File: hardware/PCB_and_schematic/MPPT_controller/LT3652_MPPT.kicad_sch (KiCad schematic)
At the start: 36 parts, among them J10 RS485, J8 ICP, J9 Conn_01x03, Q17 BC817, Q18 BC817, Q19 BC817, Q20 BC817, U1 LT3652EMSE, U5 TL431LP, U6 ST485

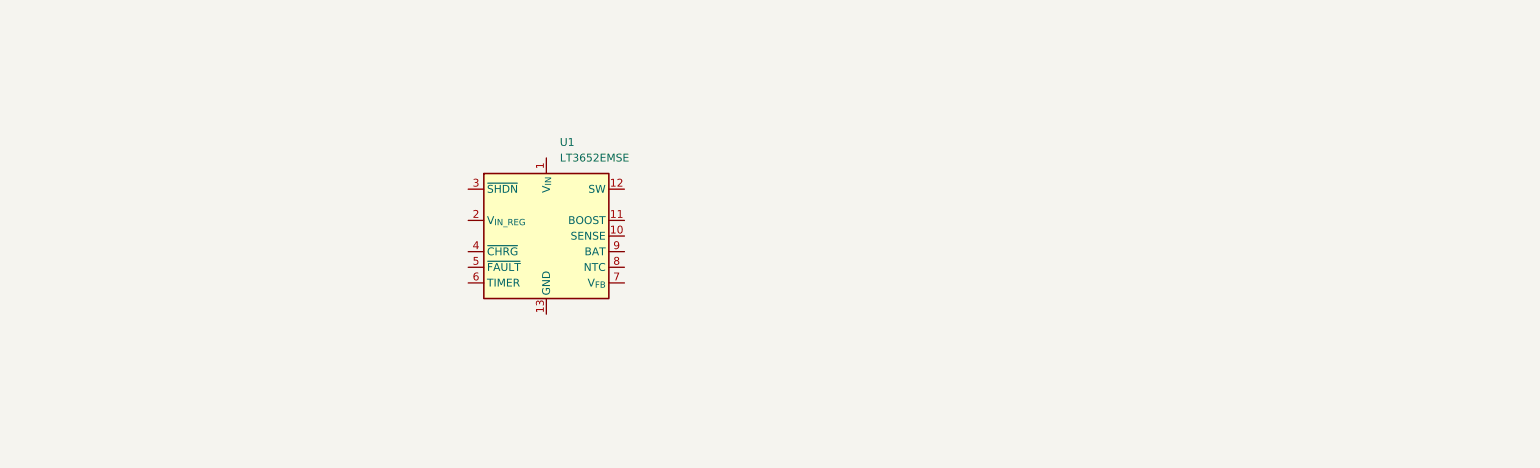
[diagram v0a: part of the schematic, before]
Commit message: MPPT LT3652 schematic uptade
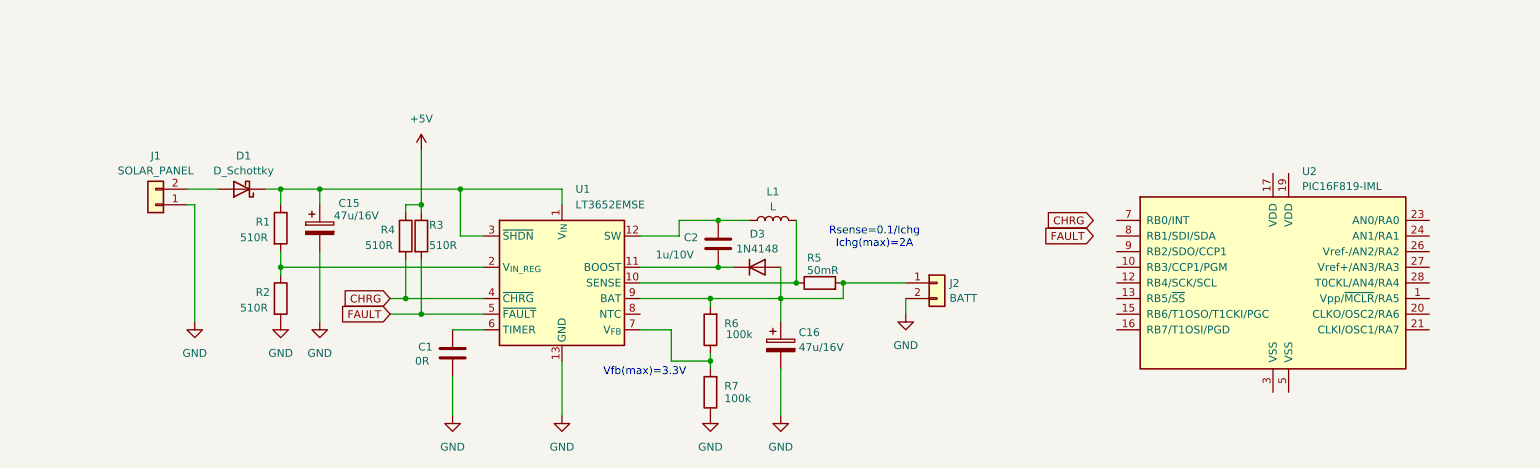
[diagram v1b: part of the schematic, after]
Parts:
- added C1: 0R, Capacitor_SMD:C_0805_2012Metric_Pad1.18x1.45mm_HandSolder, symbol Device:C
- added C15, C16: 47u/16V, symbol Device:C_Polarized
- added C2: 1u/10V, Capacitor_SMD:C_0805_2012Metric_Pad1.18x1.45mm_HandSolder, symbol Device:C
- added D1: D_Schottky, symbol Device:D_Schottky
- added D3: 1N4148, Diode_THT:D_DO-35_SOD27_P7.62mm_Horizontal, symbol Diode:1N4148
- added J1: SOLAR_PANEL, symbol Connector_Generic:Conn_01x02
- added J2: BATT, symbol Connector_Generic:Conn_01x02
- added L1: L, symbol Device:L
- added R1, R2, R3, R4: 510R, Resistor_SMD:R_0805_2012Metric_Pad1.20x1.40mm_HandSolder, symbol Device:R
- added R5: 50mR, Resistor_SMD:R_0805_2012Metric_Pad1.20x1.40mm_HandSolder, symbol Device:R
- added R6, R7: 100k, Resistor_SMD:R_0805_2012Metric_Pad1.20x1.40mm_HandSolder, symbol Device:R
- added U2: PIC16F819-IML, symbol MCU_Microchip_PIC16:PIC16F819-IML
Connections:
- net +5V: now also R3.1, R4.1
- net GND: now also U1.13 (GND), C1.2, C15.2, C16.2, J1.1 (Pin_1), J2.2 (Pin_2), R2.2, R7.1
- net at U1.1 (V_{IN}): now also U1.3 (~{SHDN}), C15.1, D1.1 (K), R1.1
- net at U1.10 (SENSE): now also L1.2, R5.1
- net at U1.11 (BOOST): now also C2.2, D3.1 (K)
- net at U1.12 (SW): now also C2.1, L1.1
- net at U1.2 (V_{IN_REG}): now also R1.2, R2.1
- net CHRG: now reaches U1.4 (~{CHRG})
- net CHRG: now also R4.2
- net FAULT: now reaches U1.5 (~{FAULT})
- net FAULT: now also R3.2
- net at U1.6 (TIMER): now also C1.1
- net at U1.7 (V_{FB}): now also R6.1, R7.2
- net at U1.9 (BAT): now also C16.1, D3.2 (A), J2.1 (Pin_1), R5.2, R6.2
- new net: D1.2 (A), J1.2 (Pin_2)
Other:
- note added: "Rsense=0.1/Ichg Ichg(max)=2A"
- note added: "Vfb(max)=3.3V"
- moved on the sheet: U1

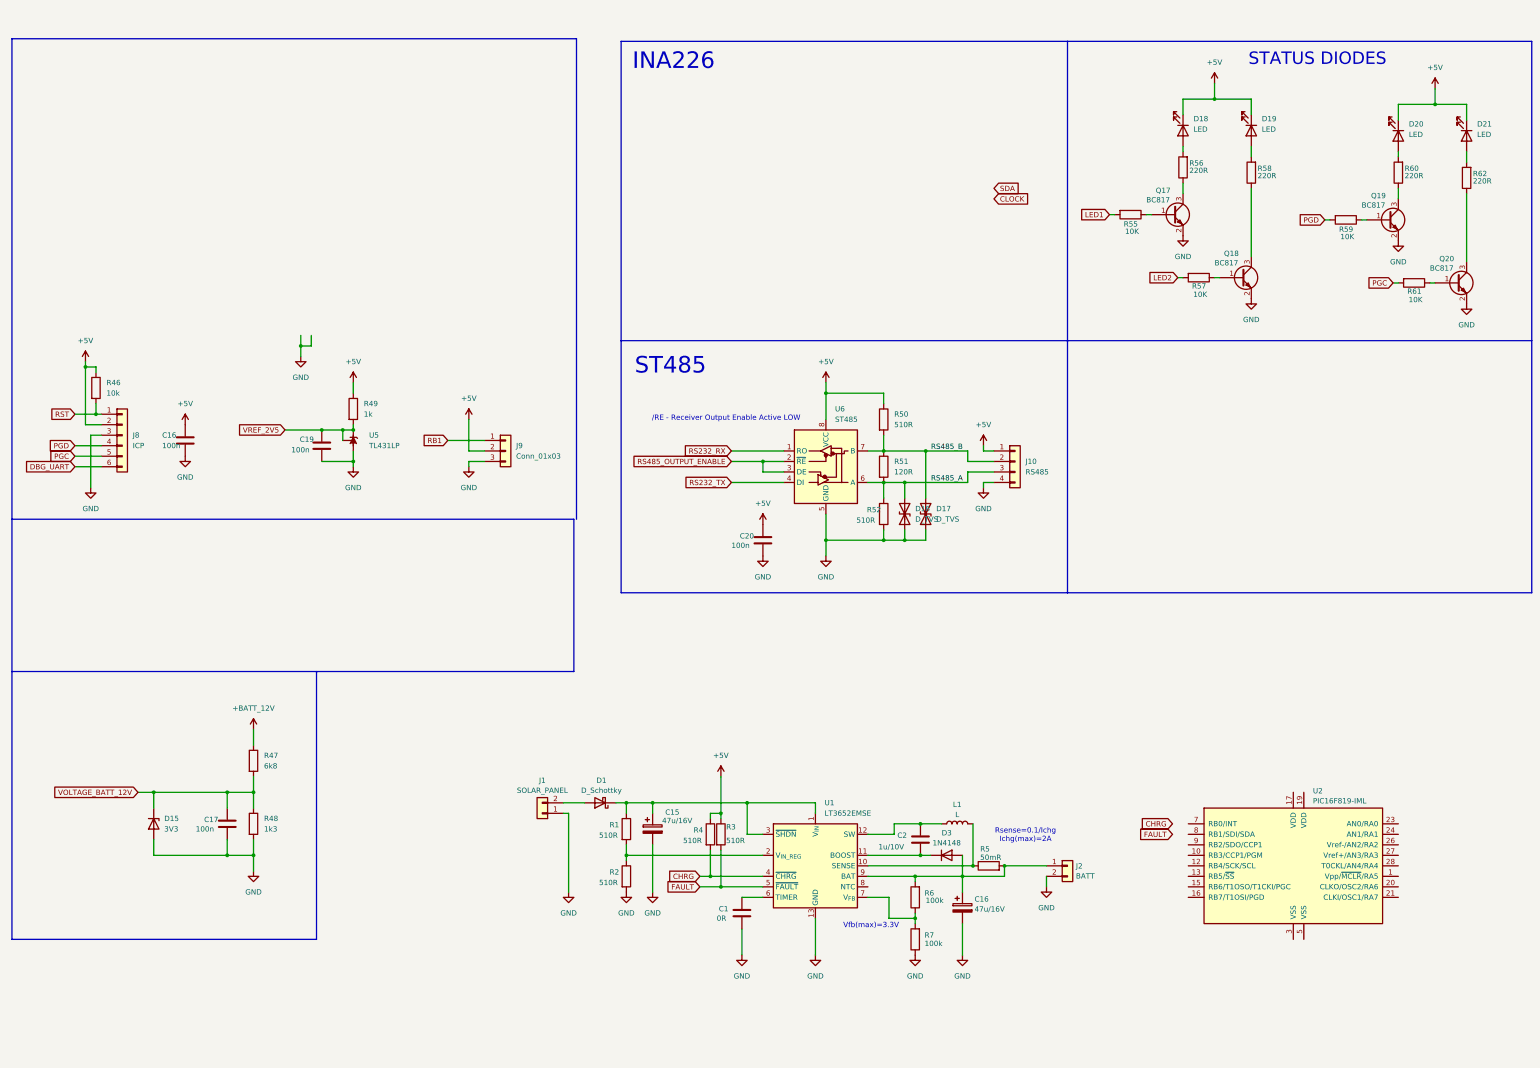
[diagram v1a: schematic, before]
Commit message: lt3252 circut simulation and update schematic
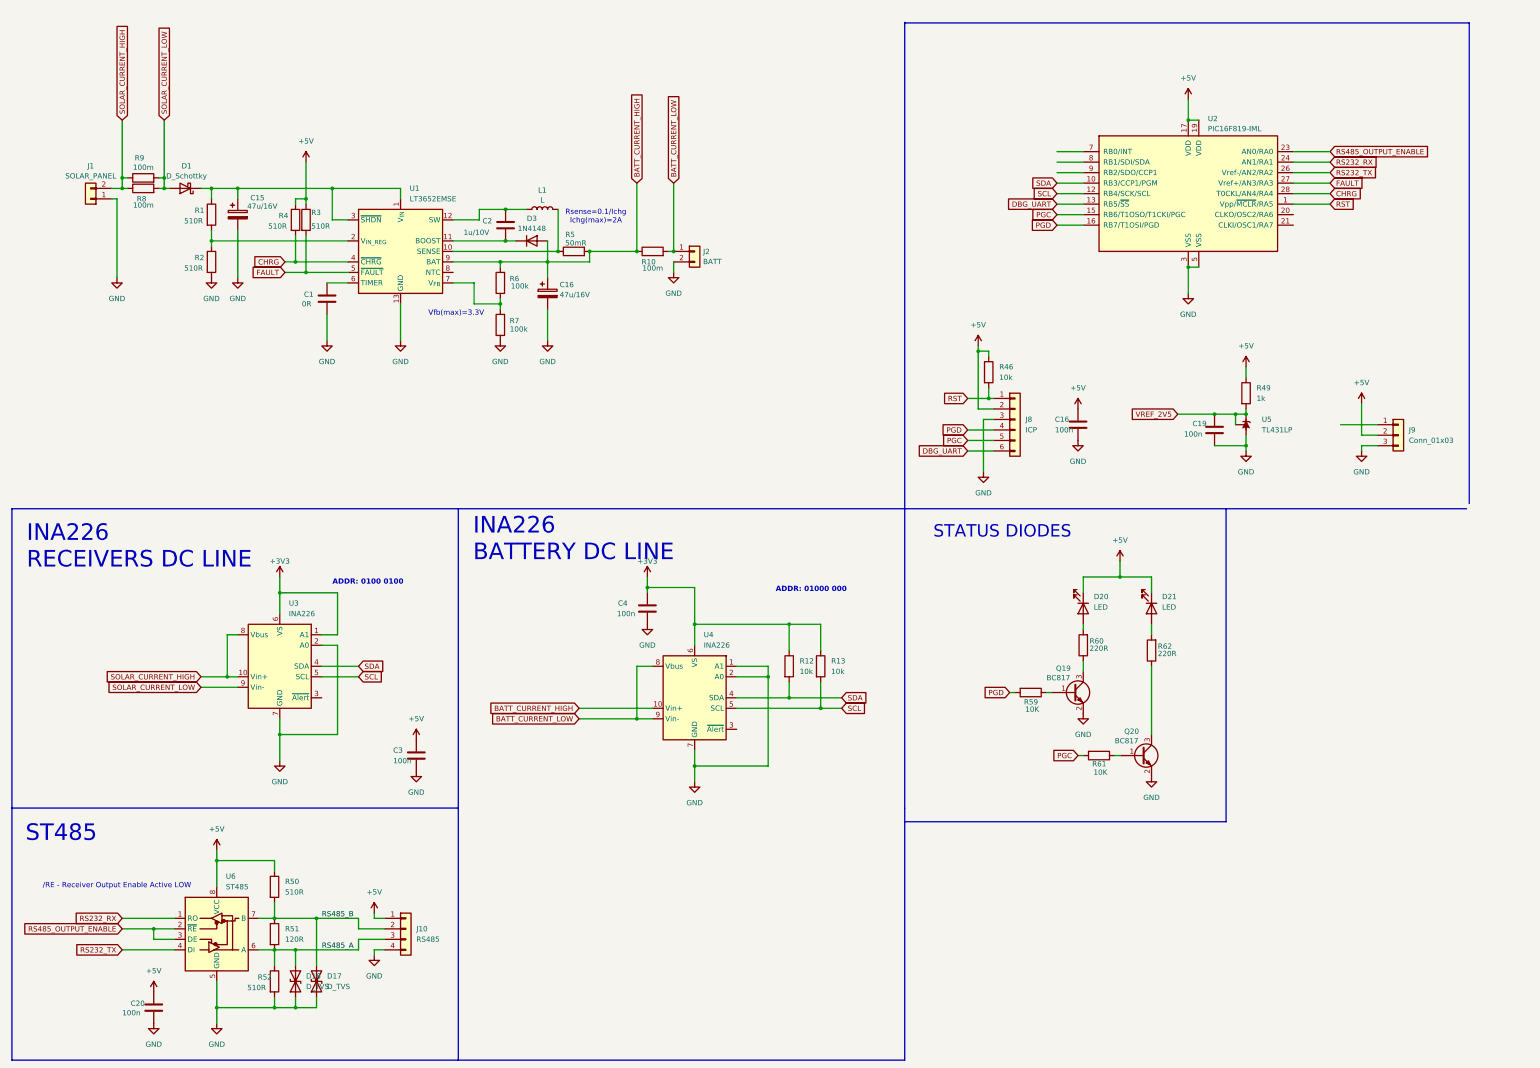
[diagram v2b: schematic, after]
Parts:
- removed C17: 100n, Capacitor_SMD:C_0805_2012Metric_Pad1.18x1.45mm_HandSolder, symbol Device:C
- removed D15: 3V3, Diode_SMD:D_MiniMELF, symbol Device:D_Zener
- removed D18, D19: LED, LED_THT:LED_D5.0mm, symbol Device:LED
- removed Q17, Q18: BC817, Package_TO_SOT_SMD:SOT-23, symbol Transistor_BJT:BC817
- removed R47: 6k8, Resistor_SMD:R_0805_2012Metric_Pad1.20x1.40mm_HandSolder, symbol Device:R
- removed R48: 1k3, Resistor_SMD:R_0805_2012Metric_Pad1.20x1.40mm_HandSolder, symbol Device:R
- removed R55, R57: 10K, Resistor_SMD:R_0805_2012Metric_Pad1.20x1.40mm_HandSolder, symbol Device:R
- removed R56, R58: 220R, Resistor_SMD:R_0805_2012Metric_Pad1.20x1.40mm_HandSolder, symbol Device:R
- added C3, C4: 100n, Resistor_SMD:R_0805_2012Metric_Pad1.20x1.40mm_HandSolder, symbol Device:C
- added R10, R8, R9: 100m, Resistor_SMD:R_0805_2012Metric_Pad1.20x1.40mm_HandSolder, symbol Device:R
- added R12, R13: 10k, Resistor_SMD:R_0805_2012Metric_Pad1.20x1.40mm_HandSolder, symbol Device:R
- added U3, U4: INA226, Package_SO:VSSOP-10_3x3mm_P0.5mm, symbol Sensor_Energy:INA226
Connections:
- net +5V: now also U2.17 (VDD), U2.19 (VDD), C3.1
- net CHRG: now also U2.28 (T0CKL/AN4/RA4)
- net DBG_UART: now also U2.13 (RB5/~{SS})
- net FAULT: now also U2.27 (Vref+/AN3/RA3)
- net GND: now also U2.3 (VSS), U2.5 (VSS), C3.2, C4.2, U3.2 (A0), U3.7 (GND), U4.1 (A1), U4.2 (A0), U4.7 (GND)
- net PGC: now also U2.15 (RB6/T1OSO/T1CKI/PGC)
- net PGD: now also U2.16 (RB7/T1OSI/PGD)
- net RS232_RX: now also U2.24 (AN1/RA1)
- net RS232_TX: now also U2.26 (Vref-/AN2/RA2)
- net RS485_OUTPUT_ENABLE: now also U2.23 (AN0/RA0)
- net RST: now also U2.1 (Vpp/~{MCLR}/RA5)
- net SDA: now also U2.10 (RB3/CCP1/PGM), R12.2, U3.4 (SDA), U4.4 (SDA)
- net SOLAR_CURRENT_HIGH: now reaches J1.2 (Pin_2)
- net SOLAR_CURRENT_HIGH: now also R8.1, R9.1, U3.10 (Vin+), U3.8 (Vbus); no longer D1.2 (A)
- net BATT_CURRENT_HIGH: now reaches C16.1, D3.2 (A), R5.2, R6.2, U1.9 (BAT)
- net BATT_CURRENT_HIGH: now also R10.1, U4.10 (Vin+); no longer J2.1 (Pin_1)
- net SCL: now reaches U2.12 (RB4/SCK/SCL)
- net SCL: now also R13.2, U3.5 (SCL), U4.5 (SCL)
- net RB1: no longer names the net of J9.1 (Pin_1)
- new net +3V3: C4.1, R12.1, R13.1, U3.1 (A1), U3.6 (VS), U4.6 (VS)
- new net BATT_CURRENT_LOW: J2.1 (Pin_1), R10.2, U4.8 (Vbus), U4.9 (Vin-)
- new net SOLAR_CURRENT_LOW: D1.2 (A), R8.2, R9.2, U3.9 (Vin-)
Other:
- note added: "ADDR: 0100 0100"
- note added: "ADDR: 01000 000"
- note added: "INA226 BATTERY DC LINE"
- note added: "INA226 RECEIVERS DC LINE"
- note removed: "INA226"
- moved on the sheet: C1, C15, C16, C19, C2, C20, D1, D16, D17, D20, D21, D3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

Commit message: Splitter PCB, connectors esp board
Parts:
- removed C19: 100n, Capacitor_SMD:C_0805_2012Metric_Pad1.18x1.45mm_HandSolder, symbol Device:C
- removed J9: Conn_01x03, Connector_PinHeader_2.54mm:PinHeader_1x03_P2.54mm_Vertical, symbol Connector_Generic:Conn_01x03
- removed R49: 1k, Resistor_SMD:R_0805_2012Metric_Pad1.20x1.40mm_HandSolder, symbol Device:R
- removed U5: TL431LP, Package_TO_SOT_THT:TO-92_Inline, symbol Reference_Voltage:TL431LP
- added C5, C6: 100n, Resistor_SMD:R_0805_2012Metric_Pad1.20x1.40mm_HandSolder, symbol Device:C
- added C7: 100u/6,3V, symbol Device:C_Polarized
- added C8: 470u/16V, symbol Device:C_Polarized
- added C9: 100n, Capacitor_SMD:C_0805_2012Metric_Pad1.18x1.45mm_HandSolder, symbol Device:C
- added D2, D4, D5: LED, LED_THT:LED_D5.0mm, symbol Device:LED
- added J3: LCD_DISPLAY, symbol Connector_Generic:Conn_01x05
- added J4, J5: THERMISTOR, symbol Connector_Generic:Conn_01x02
- added Q1, Q2, Q3: BC817, Package_TO_SOT_SMD:SOT-23, symbol Transistor_BJT:BC817
- added R11: 1k, Resistor_SMD:R_0805_2012Metric_Pad1.20x1.40mm_HandSolder, symbol Device:R
- added R14, R16, R17: 10K, Resistor_SMD:R_0805_2012Metric_Pad1.20x1.40mm_HandSolder, symbol Device:R
- added R15, R18, R21: 220R, Resistor_SMD:R_0805_2012Metric_Pad1.20x1.40mm_HandSolder, symbol Device:R
- added R19, R20: 100K, Resistor_SMD:R_0805_2012Metric_Pad1.20x1.40mm_HandSolder, symbol Device:R
- added U5: LM358, symbol Amplifier_Operational:LM358
- added U7: L7805, symbol Regulator_Linear:L7805
- added U8: TL431LP, Package_TO_SOT_THT:TO-92_Inline, symbol Reference_Voltage:TL431LP
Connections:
- net +3V3 is gone; now on net +5V: C4.1, R12.1, R13.1, U3.1 (A1), U3.6 (VS), U4.6 (VS)
- net +5V: now also C6.1, C7.1, C9.1, D2.1 (K), D4.1 (K), D5.1 (K), J3.4 (Pin_4), J4.2 (Pin_2), J5.2 (Pin_2), R11.1, U5.8 (V+), U7.3 (OUT)
- net DBG_UART: now also R17.2
- net FAULT: now also U2.7 (RB0/INT); no longer U2.27 (Vref+/AN3/RA3)
- net GND: now also C5.2, C6.2, C7.2, C8.2, C9.2, J3.5 (Pin_5), Q1.2 (E), Q2.2 (E), Q3.2 (E), R19.2, R20.2, U5.4 (V-), U7.2 (GND), U8.2 (A)
- net RS232_RX: now also R16.2
- net RS232_TX: now also R14.2
- net VREF_2V5: now also U2.27 (Vref+/AN3/RA3), R11.2, U8.1 (REF), U8.3 (K)
- net TEMP1: now reaches U2.20 (CLKO/OSC2/RA6)
- net TEMP1: now also U5.1, U5.2 (-)
- net TEMP2: now reaches U2.21 (CLKI/OSC1/RA7)
- net TEMP2: now also U5.6 (-), U5.7
- net LATCH: now reaches U2.8 (RB1/SDI/SDA)
- net LATCH: now also J3.1 (Pin_1)
- net CLOCK: now reaches U2.9 (RB2/SDO/CCP1)
- net BATT_CURRENT_LOW renamed +12V
- net +12V: now also C5.1, C8.1, U7.1 (IN)
- net SCL renamed SCL_SCK
- net SCL_SCK: now also J3.3 (Pin_3)
- new net: D2.2 (A), R15.2
- new net: Q1.1 (B), R14.1
- new net: Q1.3 (C), R15.1
- new net: J4.1 (Pin_1), R19.1, U5.3 (+)
- new net: D5.2 (A), R21.2
- new net: Q2.1 (B), R17.1
- new net: Q3.3 (C), R21.1
- new net: J5.1 (Pin_1), R20.1, U5.5 (+)
- new net: D4.2 (A), R18.2
- new net: Q2.3 (C), R18.1
- new net: Q3.1 (B), R16.1
- new net DATA: J3.2 (Pin_2)
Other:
- moved on the sheet: C1, C15, C16, C2, C4, D1, D3, J1, J2, L1, R1, R10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
